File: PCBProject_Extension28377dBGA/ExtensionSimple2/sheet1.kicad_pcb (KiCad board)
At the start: 4 copper layers, 86 parts, among them P1 Header 6X2, P2 Header 6X2, P3 Header 2X2, P4 Header 2X2, P5 Header 2X2, P6 Header 2X2, Q1 FMMT618TA, U1 SN74ABT541, U2 SN74ABT541

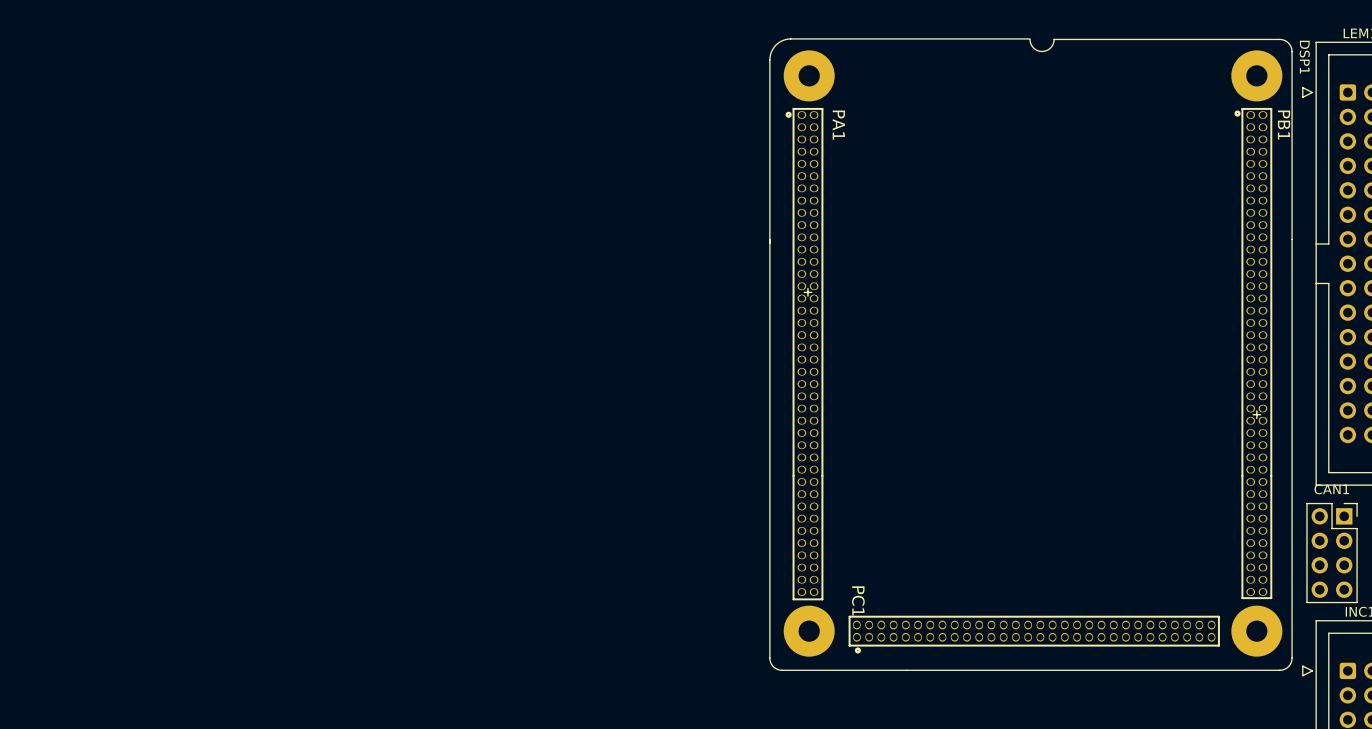
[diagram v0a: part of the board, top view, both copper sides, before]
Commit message: comnponents kayout in the pcb
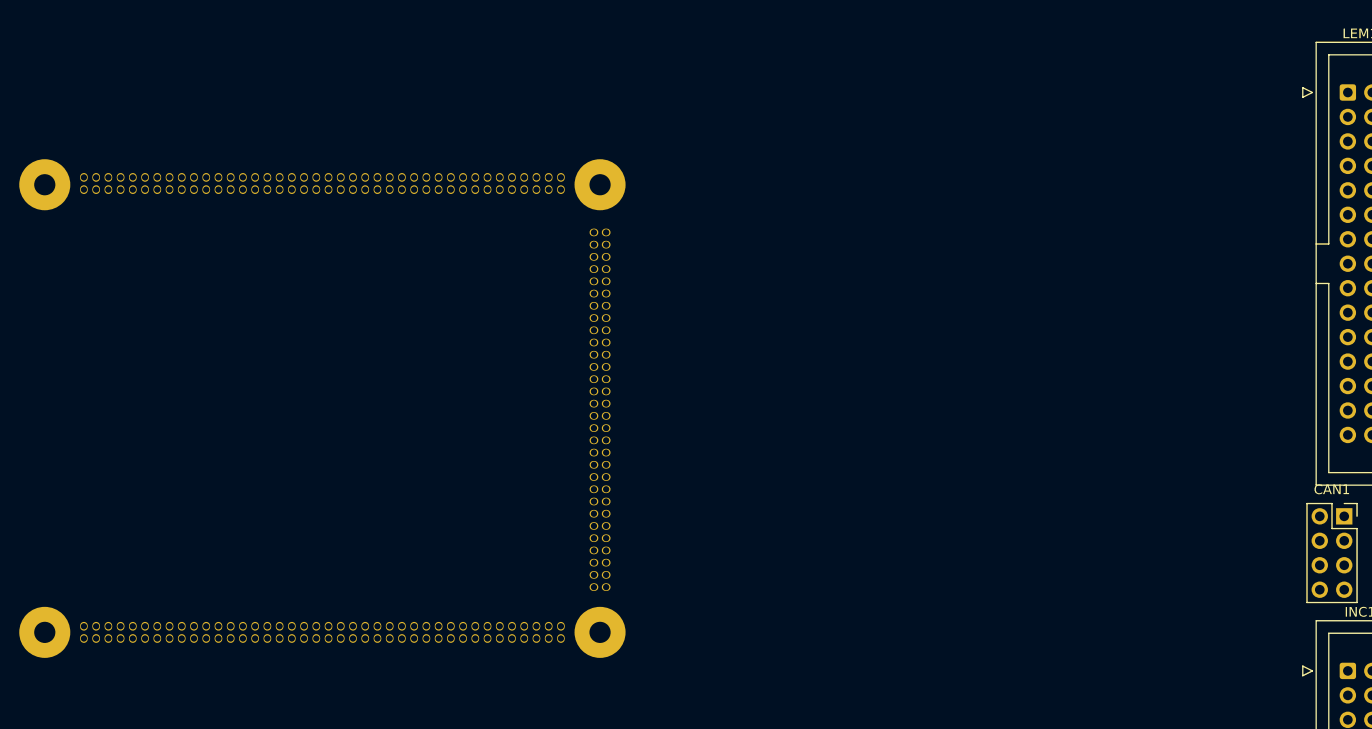
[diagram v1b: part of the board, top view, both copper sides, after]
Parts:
- DSP1: moved to B.Cu
- moved DSP1 56.7 mm to (166.6, 114.2), turned to -90 degrees

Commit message: Components layout
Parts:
- R25, R26, R27, R28, R32, R33: moved to B.Cu
- moved POWER1 131.9 mm to (129.5, 139.7)
- moved UART4 130.0 mm to (146.1, 92.7), turned to 90 degrees
- moved INC1 125.2 mm to (127.0, 88.9)
- moved R23 124.3 mm to (154.9, 80.9)
- moved R24 124.3 mm to (154.9, 83.8)
- moved RU1 116.7 mm to (177.8, 83.8)
- moved UART3 116.4 mm to (147.3, 109.2), turned to 90 degrees
- moved C12 113.8 mm to (161.6, 80.9), turned to 90 degrees
- moved DI1 113.1 mm to (148.9, 80.9)
- moved R25 112.8 mm to (139.7, 160.4), turned to 90 degrees
- moved UART2 106.8 mm to (146.1, 125.7), turned to 90 degrees
- moved LEM2 106.1 mm to (195.6, 194.8), turned to -90 degrees
- moved VDC_BUS1 105.3 mm to (279.4, 146.1), turned to 180 degrees
- moved UART1 96.9 mm to (147.3, 142.2), turned to 90 degrees
- moved C8 96.4 mm to (282.0, 114.6), turned to 90 degrees
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
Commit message: block routing done.
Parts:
- removed P3, P4, P5, P6: Header 2X2, Connector_PinSocket_2.54mm:PinSocket_2x02_P2.54mm_Vertical
- added J1: Conn_02x08_Top_Bottom, Connector_PinSocket_2.54mm:PinSocket_2x08_P2.54mm_Vertical, F.Cu at (269.2, 180.3)
- added J2: Conn_01x02_Pin, Connector_PinSocket_2.54mm:PinSocket_2x02_P2.54mm_Vertical, F.Cu at (41.9, 52.1)
- added J3: Conn_01x02_Pin, Connector_PinSocket_2.54mm:PinSocket_2x02_P2.54mm_Vertical, F.Cu at (39.4, 58.4)
- R25, R26, R27, R28, R32, R33: moved to F.Cu
- moved R13 262.7 mm to (45.7, 49.5), turned to 90 degrees
- moved R15 253.8 mm to (45.7, 61.0), turned to 90 degrees
- moved R19 252.7 mm to (48.3, 49.5), turned to 90 degrees
- moved R14 250.6 mm to (45.7, 53.3), turned to -90 degrees
- moved C5 247.8 mm to (50.8, 53.3), turned to 90 degrees
- moved R21 245.8 mm to (53.3, 45.7), turned to 90 degrees
- moved VDC_BUS1 245.7 mm to (57.1, 41.4), turned to 0 degrees
- moved R16 245.6 mm to (45.7, 57.1), turned to -90 degrees
- moved C7 245.5 mm to (50.8, 49.5), turned to 90 degrees
- moved R20 244.7 mm to (48.3, 61.0)
- moved C10 243.0 mm to (50.8, 45.7), turned to 90 degrees
- moved D1 242.6 mm to (53.3, 41.0), turned to -90 degrees
- moved R17 241.0 mm to (48.3, 53.3), turned to 90 degrees
- moved C9 240.1 mm to (55.9, 45.7)
- moved C8 237.4 mm to (50.8, 61.0)
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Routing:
- net /BootFromFlash: track 0.00 -> 20.4 mm
- net /PWM1A_5V: track 0.00 -> 17.6 mm
- net /PWM6B_5V: track 0.00 -> 15.5 mm
- net /PWM4A_5V: track 0.00 -> 15.0 mm
- net /PWM2A_5V: track 0.00 -> 15.0 mm
- net /PWM5A_5V: track 0.00 -> 12.8 mm
- net /PWM3A_5V: track 0.00 -> 12.4 mm
- net /PWM5B_5V: track 0.00 -> 12.1 mm
- net /DSP_PWM1~{_ENABL}E: track 0.00 -> 11.8 mm
- net /PWM6A_5V: track 0.00 -> 11.5 mm
- net /PWM4B_5V: track 0.00 -> 10.9 mm
- net Net-(C6-Pad2): track 0.00 -> 10.7 mm
- net /PWM1B_5V: track 0.00 -> 10.2 mm
- net /PWM3B_5V: track 0.00 -> 10.1 mm
- net /IPM_VDC_BUS2: track 0.00 -> 10.0 mm
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
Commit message: update sheet1
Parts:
- removed P1, P2: Header 6X2, Connector_PinSocket_2.54mm:PinSocket_2x06_P2.54mm_Vertical
- added IPM2: Conn_02x08_Top_Bottom, Connector_PinSocket_2.54mm:PinSocket_2x08_P2.54mm_Vertical, F.Cu at (316.0, 118.1)
- moved J2 303.2 mm to (338.5, 114.8)
- moved R13 303.2 mm to (342.3, 112.3)
- moved R14 303.2 mm to (342.3, 116.1)
- moved R15 303.2 mm to (342.3, 123.7)
- moved R16 303.2 mm to (342.3, 119.9)
- moved C10 303.2 mm to (347.4, 108.5)
- moved C11 303.2 mm to (352.5, 123.7)
- moved C5 303.2 mm to (347.4, 116.1)
- moved C6 303.2 mm to (347.4, 119.9)
- moved C7 303.2 mm to (347.4, 112.3)
- moved C8 303.2 mm to (347.4, 123.7)
- moved C9 303.2 mm to (352.5, 108.5)
- moved J3 303.2 mm to (336.0, 121.1)
- moved N1 303.2 mm to (352.5, 116.1)
- moved R17 303.2 mm to (344.9, 116.1)
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- renumbered J1 to IPM1

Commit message: extension board layout
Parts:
- added J1: Conn_02x05_Odd_Even, Connector_IDC:IDC-Header_2x05_P2.54mm_Vertical, F.Cu at (385.1, 88.4)
- added SPI1: HIF3FC-20PA-2.54DSA, Connector_IDC:IDC-Header_2x10_P2.54mm_Vertical, B.Cu at (220.4, 188.6)
- added SPI2: Conn_02x04_Counter_Clockwise, Connector_PinSocket_2.54mm:PinSocket_2x04_P2.54mm_Vertical, F.Cu at (256.7, 155.3)
- moved RU2 190.3 mm to (235.8, 234.6)
- moved RU1 190.3 mm to (235.8, 231.6)
- moved LEM2 157.2 mm to (257.0, 217.4)
- moved LEM1 125.0 mm to (220.5, 252.0)
- moved CAN1 109.8 mm to (235.9, 105.4), turned to 180 degrees
- moved UART1 101.0 mm to (247.1, 124.5)
- moved UART3 93.2 mm to (254.5, 124.5)
- moved CAN2 89.4 mm to (218.2, 105.4), turned to 180 degrees
- moved UART2 86.2 mm to (239.8, 124.5)
- moved J3 67.9 mm to (280.3, 160.1), turned to -90 degrees
- moved UART4 66.5 mm to (227.2, 105.4), turned to 180 degrees
- moved J2 60.0 mm to (280.4, 100.1)
- moved INC1 57.0 mm to (227.1, 115.8), turned to 90 degrees
- moved C10 53.8 mm to (293.6, 109.3)
- moved C5 53.8 mm to (293.6, 116.9)
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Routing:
- net /PWM6B_5V: track 15.5 -> 5.06 mm
- net /PWM5B_5V: track 12.1 -> 4.26 mm
- net /DC_BUS_2M1: track 7.25 -> 0.00 mm
- net /DSP_PWM2~{_ENABL}E: track 7.92 -> 14.8 mm
- net /GND_2M1: track 6.73 -> 0.00 mm
- net /GND_2M2: track 6.70 -> 0.00 mm
- net /DC_BUS_2M2: track 6.87 -> 0.38 mm
- net /PWM1A_5V: track 17.6 -> 11.2 mm
- net /PWM3A_5V: track 12.4 -> 6.37 mm
- net Net-(C8-Pad1): track 5.10 -> 10.8 mm
- net /PWM4B_5V: track 10.9 -> 5.25 mm
- net /PWM1B_5V: track 10.2 -> 4.79 mm
- net /PWM2B_5V: track 9.46 -> 4.02 mm
- net /PWM3B_5V: track 10.1 -> 5.02 mm
- net /PWM2A_5V: track 15.0 -> 10.2 mm
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
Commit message: HY加油
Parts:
- added RU3: 0R, Resistor_SMD:R_0805_2012Metric, F.Cu at (226.8, 158.5)
- C1, C12, C2, C3, C4, R1, R10, R11, R12, R2, R23, R24, R25, R26, R27, R28, R3, R32, R33, R4, R5, R6, R7, R8, R9, U1, U2: moved to B.Cu
- DSP1: footprint 1mmlab_footprint:DSP_240 -> 1mmlab_footprint:DSP_240_SMD
- LEM1, LEM2: footprint Connector_IDC:IDC-Header_2x15_P2.54mm_Vertical -> Connector_PinSocket_2.54mm:PinSocket_2x15_P2.54mm_Vertical
- moved J1 175.2 mm to (212.4, 117.9), turned to 90 degrees
- moved LEM1 172.6 mm to (270.4, 86.8), turned to -90 degrees
- moved RU1 141.8 mm to (243.4, 90.1), turned to 180 degrees
- moved TP12 110.5 mm to (389.5, 144.3), turned to -90 degrees
- moved TP10 106.2 mm to (386.5, 144.3), turned to -90 degrees
- moved TP8 101.9 mm to (383.4, 144.3), turned to -90 degrees
- moved TP6 97.6 mm to (380.4, 144.3), turned to -90 degrees
- moved TP4 93.4 mm to (377.3, 144.3), turned to -90 degrees
- moved RU2 89.4 mm to (244.4, 145.6), turned to 180 degrees
- moved TP2 89.1 mm to (374.3, 144.3), turned to -90 degrees
- moved LEM2 82.9 mm to (211.2, 148.4), turned to 90 degrees
- moved IPM1 70.4 mm to (245.5, 114.6), turned to 180 degrees
- moved C2 69.8 mm to (279.1, 149.1)
- moved C4 69.8 mm to (283.7, 149.1)
- moved R2 69.8 mm to (274.2, 149.1)
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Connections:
- J1 pad 1: unconnected-(J1-Pin_1-Pad1) -> /QEP1_HALL_U
- J1 pad 10: unconnected-(J1-Pin_10-Pad10) -> D+5V
- J1 pad 2: unconnected-(J1-Pin_2-Pad2) -> /MQEP1A
- J1 pad 3: unconnected-(J1-Pin_3-Pad3) -> /QEP1_HALL_V
- J1 pad 4: unconnected-(J1-Pin_4-Pad4) -> /MQEP1B
- J1 pad 5: unconnected-(J1-Pin_5-Pad5) -> /QEP1_HALL_W
- J1 pad 6: unconnected-(J1-Pin_6-Pad6) -> /MQEP1Z
- J1 pad 7: unconnected-(J1-Pin_7-Pad7) -> PE_GND
- J1 pad 8: unconnected-(J1-Pin_8-Pad8) -> VDD
- J1 pad 9: unconnected-(J1-Pin_9-Pad9) -> AGND
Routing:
- net 12VGND: track 0.00 -> 135.8 mm
- net AGND: track 0.05 -> 58.2 mm
- net /BootFromFlash: track 20.4 -> 0.67 mm
- net -12: track 0.00 -> 12.7 mm
- net +12: track 0.00 -> 12.7 mm
- net /PWM4A_5V: track 11.8 -> 0.00 mm
- net /PWM1A_5V: track 11.2 -> 0.00 mm
- net /PWM2A_5V: track 10.2 -> 0.00 mm
- net /PWM5A_5V: track 9.39 -> 0.00 mm
- net Net-(LEM2-Pad7): track 0.00 -> 8.04 mm
- net A+5V: track 0.00 -> 7.62 mm
- net /PWM6A_5V: track 6.99 -> 0.00 mm
- net /PWM3A_5V: track 6.37 -> 0.00 mm
- net Net-(DI1-Pin_3): track 6.10 -> 0.00 mm
- net /DSP_PWM2~{_ENABL}E: track 14.8 -> 9.20 mm
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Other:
- board text added: "URAT4"

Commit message: Revert "HY加油"
This reverts commit aaa1912d429fb000e99d7c8797d7335188b5b639.

rollback
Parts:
- C12, R23, R24, R25, R26, R27, R28, R32, R33: moved to F.Cu
- TP1, TP10, TP11, TP12, TP2, TP3, TP4, TP5, TP6, TP7, TP8, TP9: moved to B.Cu
- moved J1 175.2 mm to (385.1, 88.4), turned to 0 degrees
- moved LEM1 172.6 mm to (220.5, 252.0), turned to 90 degrees
- moved RU1 141.8 mm to (235.8, 231.6), turned to 0 degrees
- moved TP12 101.4 mm to (303.6, 90.3), turned to 0 degrees
- moved TP10 100.6 mm to (303.6, 87.3), turned to 0 degrees
- moved TP8 99.9 mm to (303.6, 84.2), turned to 0 degrees
- moved TP6 99.4 mm to (303.6, 81.2), turned to 0 degrees
- moved TP4 99.0 mm to (303.6, 78.1), turned to 0 degrees
- moved TP2 98.9 mm to (303.6, 75.1), turned to 0 degrees
- moved RU2 89.4 mm to (235.8, 234.6), turned to 0 degrees
- moved LEM2 82.9 mm to (257.0, 217.4), turned to -90 degrees
- moved IPM1 70.4 mm to (312.4, 136.5), turned to 0 degrees
- moved J3 69.3 mm to (280.3, 160.1), turned to -90 degrees
- moved R10 66.0 mm to (288.8, 76.6)
- moved R4 66.0 mm to (288.8, 82.7)
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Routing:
- net 12VGND: track 135.8 -> 0.00 mm
- net AGND: track 58.2 -> 0.05 mm
- net /BootFromFlash: track 0.67 -> 20.4 mm
- net /PWM4A_5V: track 0.00 -> 18.6 mm
- net /PWM1A_5V: track 0.00 -> 18.2 mm
- net /PWM5A_5V: track 0.00 -> 16.4 mm
- net /PWM2A_5V: track 0.00 -> 16.0 mm
- net /PWM6A_5V: track 0.00 -> 14.2 mm
- net /PWM3A_5V: track 0.00 -> 13.9 mm
- net /PWM3B_5V: track 0.00 -> 13.1 mm
- net /PWM6B_5V: track 0.00 -> 12.9 mm
- net -12: track 12.7 -> 0.00 mm
- net +12: track 12.7 -> 0.00 mm
- net /PWM4B_5V: track 0.00 -> 12.7 mm
- net /PWM1B_5V: track 0.00 -> 12.4 mm
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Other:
- board text removed: "URAT4"

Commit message: Power layout
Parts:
- C10, C11, C12, C5, C6, C7, C8, C9, D1, D2, D3, N1, Q1, R13, R14, R15, R16, R17, R18, R19, R20, R21, R22, R23, R24, R25, R26, R27, R28, R29, R30, R31, R32, R33, VDC_BUS1, VDC_BUS2: moved to B.Cu
- moved RU2 139.3 mm to (203.7, 99.1)
- moved LEM2 135.6 mm to (230.3, 84.5)
- moved RU1 127.6 mm to (203.7, 108.1)
- moved J1 118.8 mm to (266.4, 83.0), turned to -90 degrees
- moved RU3 104.9 mm to (201.1, 103.8), turned to 180 degrees
- moved LEM1 103.9 mm to (197.1, 150.7)
- moved TP2 83.0 mm to (282.8, 155.4), turned to 180 degrees
- moved J3 82.6 mm to (306.1, 81.6), turned to 90 degrees
- moved R12 81.9 mm to (297.6, 156.0), turned to 180 degrees
- moved R10 77.8 mm to (297.6, 153.9), turned to 180 degrees
- moved TP4 77.1 mm to (282.8, 152.4), turned to 180 degrees
- moved R8 73.8 mm to (297.6, 151.9), turned to 180 degrees
- moved TP6 71.3 mm to (282.8, 149.4), turned to 180 degrees
- moved R6 69.7 mm to (297.6, 149.9), turned to 180 degrees
- moved R4 65.7 mm to (297.6, 147.8), turned to 180 degrees
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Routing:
- net AGND: track 0.05 -> 759.8 mm, vias 0 -> 3
- net D+5V: track 4.23 -> 228.7 mm, vias 0 -> 2
- net AVDD: track 0.00 -> 183.7 mm, vias 0 -> 1
- net +12: track 0.00 -> 170.1 mm
- net 12VGND: track 0.00 -> 160.6 mm
- net A+5V: track 0.00 -> 139.9 mm, vias 0 -> 2
- net -12: track 0.00 -> 126.3 mm
- net A-5V: track 0.00 -> 115.3 mm
- net /IPM_IW2: track 0.00 -> 93.4 mm, vias 0 -> 1
- net D12V1: track 0.00 -> 92.2 mm, vias 0 -> 2
- net /IPM_IU2: track 0.00 -> 90.2 mm, vias 0 -> 1
- net /IPM_IV2: track 0.00 -> 88.5 mm, vias 0 -> 1
- net /IPM_IU1: track 0.00 -> 68.6 mm
- net Net-(LEM1-Pad7): track 0.00 -> 61.3 mm, vias 0 -> 2
- net D12VGND: track 0.00 -> 52.4 mm
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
